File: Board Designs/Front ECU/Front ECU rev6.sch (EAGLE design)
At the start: 84 parts, among them IC2 OKI-78SR, IC3 OKI-78SR, X1 CONNECTOR-4, X2 CONNECTOR-4, X3 CONNECTOR-4MX150L_VERTICAL-4, X4 CONNECTOR-10MX150L_VERTICAL-10, X5 CONNECTOR-10MX150L_VERTICAL-10, X6 CONNECTOR-10MX150L_VERTICAL-10

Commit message: Add accelerometer to Front ECU
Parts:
- added C10, C11, C12, C9: 100nF, HyTechDevices:CAP0805
- added U$24: SCA3100-D04, HyTechDevices:SCA3100-D04
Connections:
- net MCP3208_CS renamed CS_MCP3208
- removed net MCP3208_MISO: U$1.D12, U$18.DOUT
- removed net MCP3208_MOSI: U$1.D11, U$18.DIN
- removed net MCP3208_SCK: U$1.D13, U$18.CLK
- new net 3.3V+: C10.2, C12.2, U$1.3.3V, U$24.DVIO, U$24.VDD
- new net CS_SCA3100: U$1.A5, U$24.CSB
- new net MISO_TEENSY: U$1.D12, U$18.DOUT, U$24.MISO
- new net MOSI_TEENSY: U$1.D11, U$18.DIN, U$24.MOSI
- new net N$10: C9.2, U$24.A_EXTC
- new net SCK_TEENSY: U$1.D13, U$18.CLK, U$24.SCK
- net GND: now also C10.1, C11.1, C12.1, C9.1, U$24.AVSS, U$24.DVSS, U$24.EMC_GND
- net N$13: now also C11.2, U$24.D_EXTC
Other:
- moved on the sheet: BUTTON, C1, C2, C3, C4, C5, C6, C7, C8, CRYSTAL, D3, IC2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

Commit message: Add 15-pin .1" header to library, update copper rubout instructions on Enerdel board, add cooling control mosfet part numbers to Rear ECU schematic, fix silkscreen fuse names in Front ECU rev6
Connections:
- net +5V: no longer U$4.VINB-
- net GND: now also R1.1
- net N$1: now also R2.2; no longer U$4.VINB+
- net N$9: now also R1.2, R2.1, U$12.VINB+
- net READ_FAULT: now also U$12.VINB-, U$12.VOUTB; no longer U$4.VOUTB
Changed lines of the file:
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@@
 <part name="P+4" library="supply1" deviceset="+12V" device=""/>
 <part name="BSPD_ENABLE" library="HyTechDevices" deviceset="M02" device="" value="JUMPER"/>
+<part name="R1" library="HyTechDevices" deviceset="RESISTOR" device="0805-RES" value="12k"/>
+<part name="R2" library="HyTechDevices" deviceset="RESISTOR" device="0805-RES" value="43k"/>
+<part name="GND7" library="HyTechSymbols" deviceset="GND" device=""/>
 </parts>
 <sheets>
@@
 <instance part="R6" gate="G$1" x="68.58" y="50.8"/>
 <instance part="P+3" gate="1" x="48.26" y="58.42" rot="R270"/>
-<instance part="P+7" gate="1" x="81.28" y="38.1" rot="R270"/>
+<instance part="P+7" gate="1" x="78.74" y="38.1" rot="R270"/>
 <instance part="P+8" gate="1" x="12.7" y="48.26" rot="R90"/>
 <instance part="U$10" gate="G$1" x="-63.5" y="17.78"/>
@@
 <instance part="P+4" gate="1" x="139.7" y="43.18" rot="R270"/>
 <instance part="BSPD_ENABLE" gate="G$1" x="58.42" y="60.96" rot="MR270"/>
+<instance part="R1" gate="G$1" x="86.36" y="-2.54"/>
+<instance part="R2" gate="G$1" x="101.6" y="-2.54"/>
+<instance part="GND7" gate="1" x="76.2" y="-2.54" rot="R270"/>
 </instances>
 <busses>
@@
 <pinref part="GND16" gate="1" pin="GND"/>
 <wire x1="5.08" y1="-2.54" x2="7.62" y2="-2.54" width="0.1524" layer="91"/>
+</segment>
+<segment>
+<pinref part="R1" gate="G$1" pin="1"/>
+<pinref part="GND7" gate="1" pin="GND"/>
+<wire x1="78.74" y1="-2.54" x2="81.28" y2="-2.54" width="0.1524" layer="91"/>
 </segment>
 </net>
@@
 <pinref part="U$4" gate="G$1" pin="VDD"/>
 <pinref part="P+7" gate="1" pin="+5V"/>
-<wire x1="78.74" y1="38.1" x2="76.2" y2="38.1" width="0.1524" layer="91"/>
-<pinref part="U$4" gate="G$1" pin="VINB-"/>
 <wire x1="76.2" y1="38.1" x2="73.66" y2="38.1" width="0.1524" layer="91"/>
-<wire x1="76.2" y1="33.02" x2="73.66" y2="33.02" width="0.1524" layer="91"/>
-<wire x1="76.2" y1="33.02" x2="76.2" y2="38.1" width="0.1524" layer="91"/>
-<junction x="76.2" y="38.1"/>
 </segment>
 <segment>
@@
 <wire x1="116.84" y1="68.58" x2="116.84" y2="55.88" width="0.1524" layer="91"/>
 <junction x="116.84" y="55.88"/>
-<pinref part="U$4" gate="G$1" pin="VINB+"/>
-<wire x1="109.22" y1="30.48" x2="109.22" y2="45.72" width="0.1524" layer="91"/>
-<wire x1="73.66" y1="30.48" x2="109.22" y2="30.48" width="0.1524" layer="91"/>
+<wire x1="109.22" y1="45.72" x2="109.22" y2="-2.54" width="0.1524" layer="91"/>
+<pinref part="R2" gate="G$1" pin="2"/>
+<wire x1="109.22" y1="-2.54" x2="106.68" y2="-2.54" width="0.1524" layer="91"/>
 </segment>
 </net>
@@
 <net name="READ_FAULT" class="0">
 <segment>
-<label x="83.82" y="35.56" size="1.778" layer="95" xref="yes"/>
-<pinref part="U$4" gate="G$1" pin="VOUTB"/>
-<wire x1="73.66" y1="35.56" x2="83.82" y2="35.56" width="0.1524" layer="91"/>
+<pinref part="U$12" gate="G$1" pin="VOUTB"/>
+<wire x1="83.82" y1="12.7" x2="86.36" y2="12.7" width="0.1524" layer="91"/>
+<wire x1="86.36" y1="12.7" x2="86.36" y2="10.16" width="0.1524" layer="91"/>
+<pinref part="U$12" gate="G$1" pin="VINB-"/>
+<wire x1="86.36" y1="10.16" x2="83.82" y2="10.16" width="0.1524" layer="91"/>
+<wire x1="86.36" y1="10.16" x2="88.9" y2="10.16" width="0.1524" layer="91"/>
+<junction x="86.36" y="10.16"/>
+<label x="88.9" y="10.16" size="1.778" layer="95" xref="yes"/>
 </segment>
 </net>
@@
 </segment>
 </net>
+<net name="N$9" class="0">
+<segment>
+<pinref part="R2" gate="G$1" pin="1"/>
+<pinref part="R1" gate="G$1" pin="2"/>
+<wire x1="96.52" y1="-2.54" x2="93.98" y2="-2.54" width="0.1524" layer="91"/>
+<pinref part="U$12" gate="G$1" pin="VINB+"/>
+<wire x1="93.98" y1="-2.54" x2="91.44" y2="-2.54" width="0.1524" layer="91"/>
+<wire x1="83.82" y1="7.62" x2="93.98" y2="7.62" width="0.1524" layer="91"/>
+<wire x1="93.98" y1="7.62" x2="93.98" y2="-2.54" width="0.1524" layer="91"/>
+<junction x="93.98" y="-2.54"/>
+</segment>
+</net>

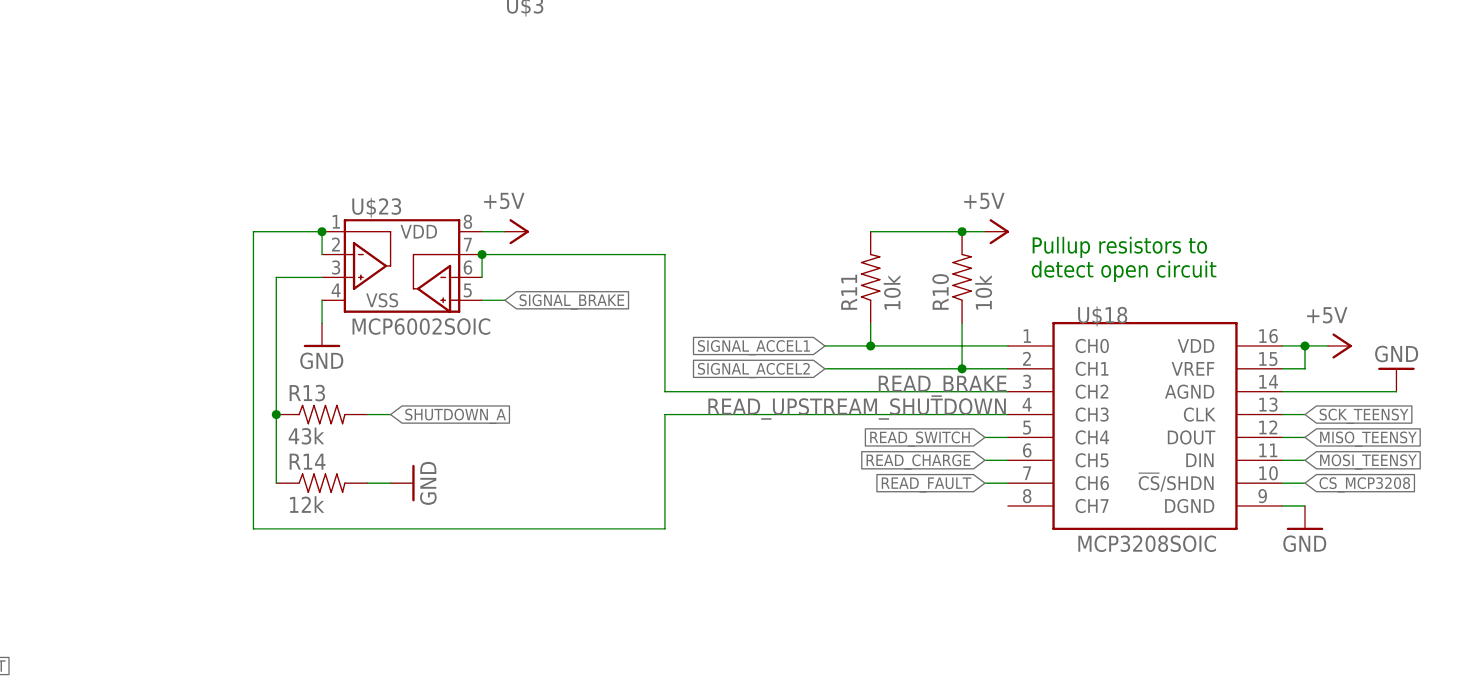
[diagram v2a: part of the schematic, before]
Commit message: Add pull-down resistors for APPS
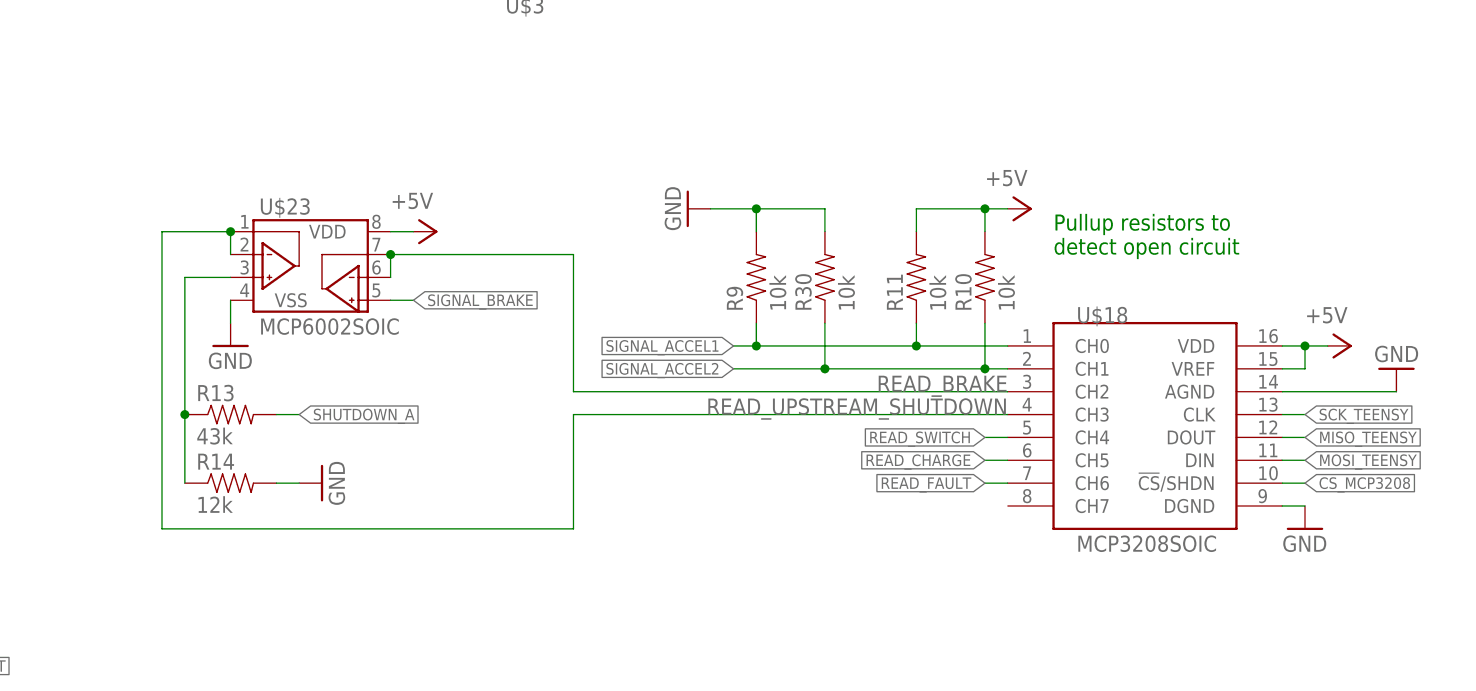
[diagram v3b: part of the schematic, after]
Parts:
- added R30, R9: 10k, HyTechDevices:RESISTOR0805-RES
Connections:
- net GND: now also R30.2, R9.2
- net N$15: now also R9.1
- net SIGNAL_ACCEL1: now also R9.1
- net SIGNAL_ACCEL2: now also R30.1
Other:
- moved on the sheet: R10, R11, R13, R14, U$23

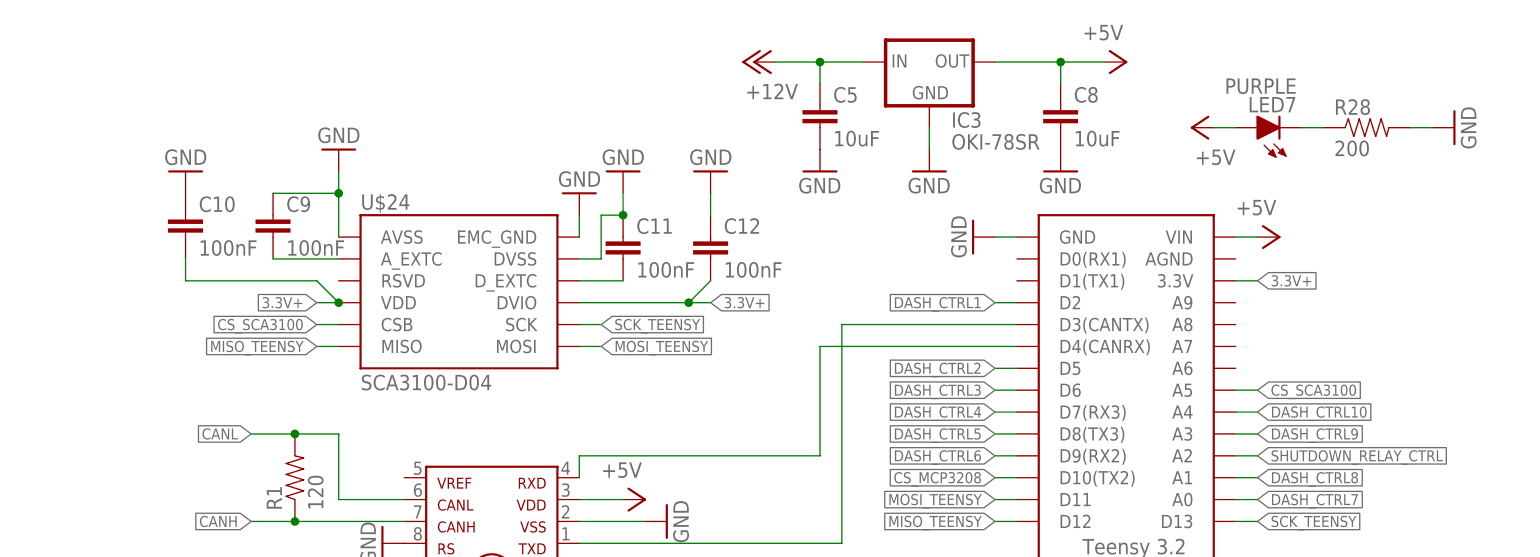
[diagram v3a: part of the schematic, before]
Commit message: Replaced murata accelerometer with ADXL345 breakout board
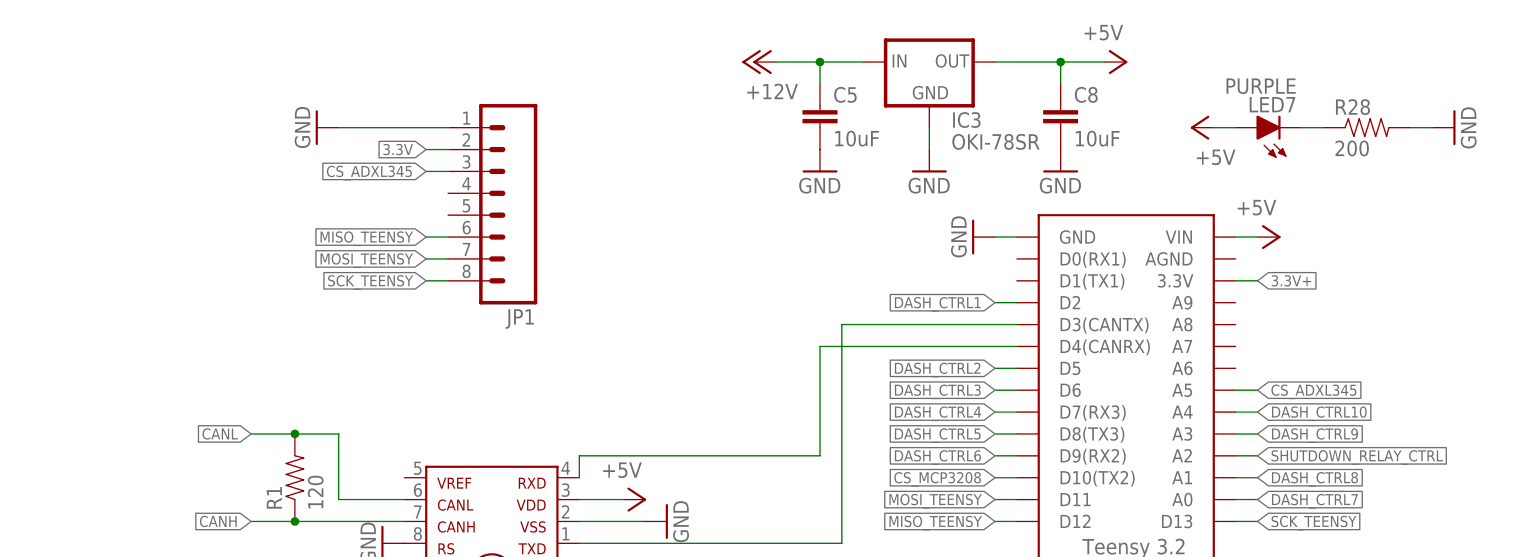
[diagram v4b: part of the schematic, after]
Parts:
- removed C10, C11, C12, C9: 100nF, HyTechDevices:CAP0805
- removed U$24: SCA3100-D04, HyTechDevices:SCA3100-D04
- added JP1: (no value), HyTechDevices:M08
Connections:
- removed net CS_SCA3100: U$1.A5, U$24.CSB
- removed net N$10: C9.2, U$24.A_EXTC
- new net 3.3V: JP1.2
- new net CS_ADXL345: JP1.3, U$1.A5
- net 3.3V+: no longer C10.2, C12.2, U$24.DVIO, U$24.VDD
- net GND: now also JP1.1; no longer C10.1, C11.1, C12.1, C9.1, U$24.AVSS, U$24.DVSS, U$24.EMC_GND
- net MISO_TEENSY: now also JP1.6; no longer U$24.MISO
- net MOSI_TEENSY: now also JP1.7; no longer U$24.MOSI
- net N$13: no longer C11.2, U$24.D_EXTC
- net SCK_TEENSY: now also JP1.8; no longer U$24.SCK
